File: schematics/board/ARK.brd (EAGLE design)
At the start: 82 x 92 mm, 82 parts, among them IC2 STM32F103C8T

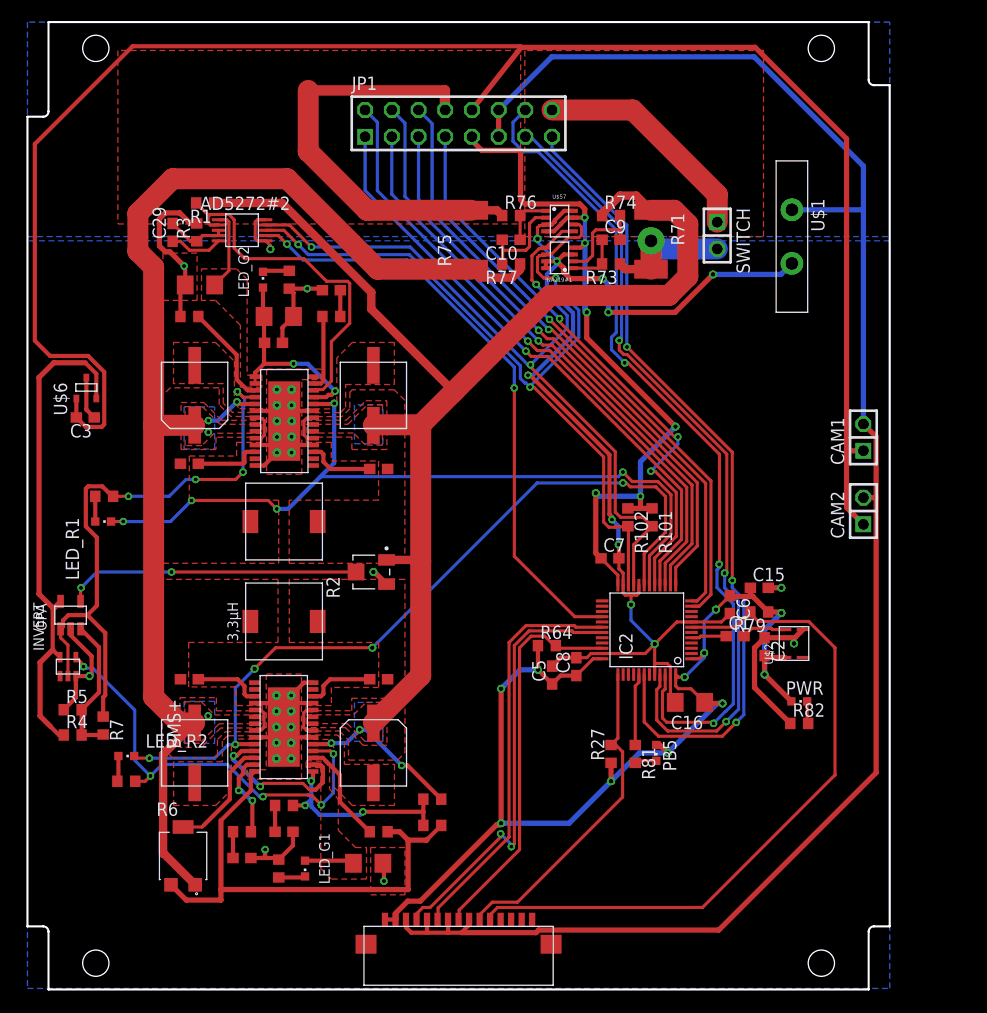
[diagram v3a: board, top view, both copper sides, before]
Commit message: Плата АРК готова к проверке
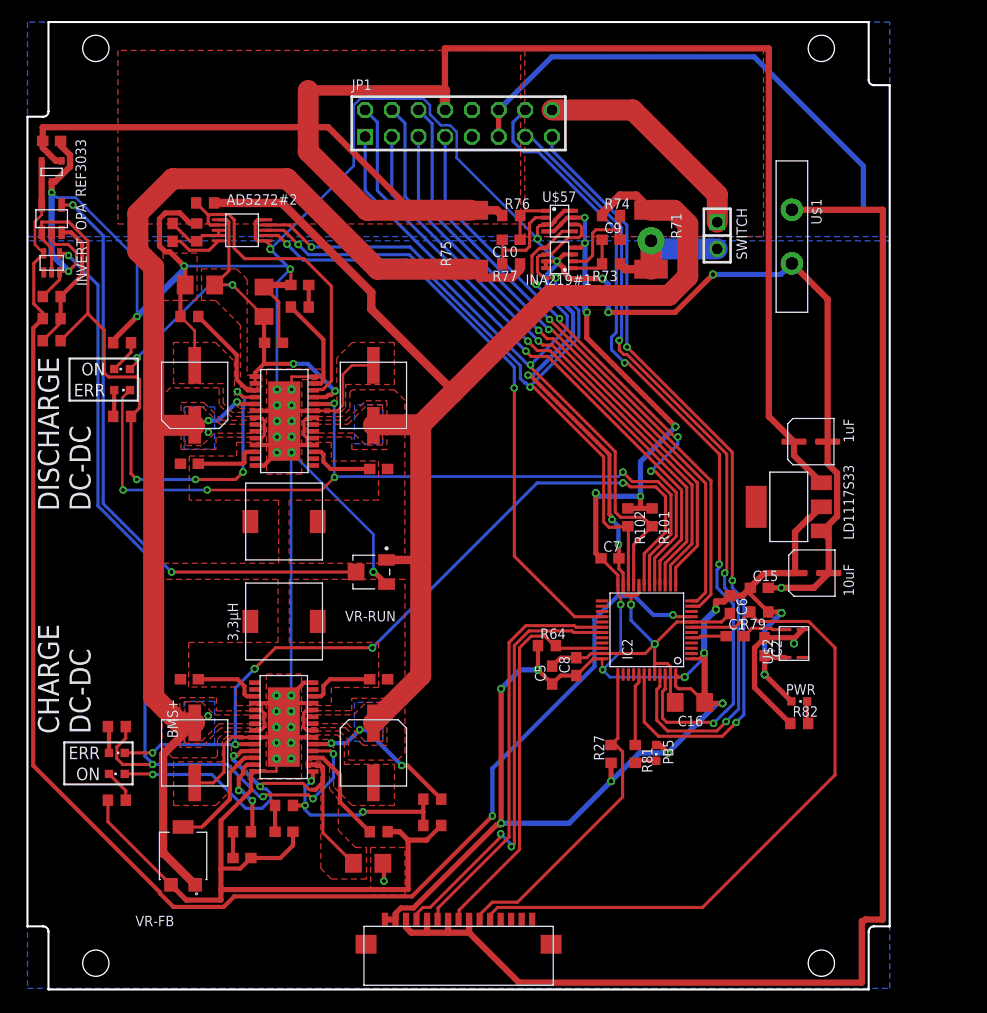
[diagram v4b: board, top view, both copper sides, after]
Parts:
- removed CAM1, CAM2: (no value), pinheadCS:1X02
- removed U$6: REF3033, CanCubeSat:SOT23-3
- added C11: 1uF, CanCubeSat:ECAP-SMD-D4
- added C4: 10uF, CanCubeSat:ECAP-SMD-D4
- added LD1117S33: LD1117S33, CanCubeSat:SOT223
- added REF3033: REF3033, CanCubeSat:SOT23-3
- moved R4 39.7 mm to (2.30, 63.8)
- moved R5 39.4 mm to (2.30, 65.9)
- moved INVERT 38.4 mm to (2.30, 69.1)
- moved OPA 37.7 mm to (2.30, 73.3)
- moved R7 36.9 mm to (2.30, 61.7), turned to 180 degrees
- moved C3 26.5 mm to (2.30, 80.7)
- moved LED_G1 20.0 mm to (8.50, 20.5), turned to 90 degrees
- moved R33 17.0 mm to (9.00, 61.5), turned to 0 degrees
- moved R100 16.7 mm to (8.50, 18.0), turned to 0 degrees
- moved LED_G2 15.9 mm to (9.00, 59.0), turned to 90 degrees
- moved LED_R1 12.6 mm to (9.00, 57.0)
- moved R32 7.79 mm to (9.00, 54.5)
- moved R57 5.28 mm to (8.50, 25.0)
- moved R30 3.13 mm to (25.9, 64.9)
- moved C52 3.04 mm to (25.9, 67.0)
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- renumbered R2 to VR-RUN, R6 to VR-FB
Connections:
- removed net 5V: C3.2, CAM1.1, CAM2.1, JP1.10, U$6.1
- new net 5V-OUT: JP1.10
- net 3V3: now also C4.P+, LD1117S33.P$3; no longer JP1.9
- net 3V3-STAB: now also REF3033.2; no longer U$6.2
- net BMS+: now also C11.P+, C3.2, LD1117S33.P$4, REF3033.1
- net GND: now also C11.P-, C4.P-, LD1117S33.P$2, REF3033.3; no longer U$6.3
- net GND-OUT: no longer CAM1.2, CAM2.2
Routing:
- net GND: track 254.5 -> 478.9 mm, vias 19 -> 20
- net 5V: track 167.7 -> 0.00 mm
- net BMS+: track 41.7 -> 162.6 mm
- net 3V3-STAB: track 47.0 -> 145.8 mm, vias 0 -> 2
- net Y: track 42.2 -> 83.6 mm
- net RUN: track 28.1 -> 57.4 mm
- net GND-OUT: track 165.9 -> 188.6 mm
- net N$234: track 20.0 -> 42.0 mm, vias 2 -> 3
- net 3V3: track 181.5 -> 199.8 mm, vias 17 -> 19
- net N$215: track 27.3 -> 43.7 mm, vias 2 -> 4
- net PGOOD2: track 75.9 -> 82.1 mm
- net A: track 57.8 -> 61.1 mm
- net N$3: track 33.3 -> 30.7 mm
- net N$81: track 7.21 -> 9.35 mm
- net N$92: track 2.54 -> 3.16 mm
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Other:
- board text added: "CHARGE DC-DC"
- board text added: "DISCHARGE DC-DC"
- board text added: "ERR"
- board text added: "ON"

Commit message: Украсил плату АРК
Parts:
- added U$3, U$4: PCB-"ARK", CanCubeSat:ITS-LOGO
- moved SWITCH 40.5 mm to (26.6, 82.7)
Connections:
- removed net 5V-OUT: JP1.10
- removed net BUSPLUS: JP1.16, SWITCH.1
- new net BMS+_OUT: JP1.8, SWITCH.1
- net BMS+: now also SWITCH.2; no longer JP1.8
- net BUS+: now also JP1.16; no longer SWITCH.2
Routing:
- net BUSPLUS: track 21.7 -> 0.00 mm
- net BUS+: track 12.5 -> 33.0 mm, vias 1 -> 2
- net BMS+_OUT: track 0.00 -> 17.5 mm
- net BMS+: track 162.6 -> 148.2 mm
- net INA_BUS+: track 131.1 -> 137.2 mm, vias 3 -> 5
- added copper zone on layer 1, net BUS+
- removed copper zone on layer 1, net BUSPLUS
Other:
- board text removed: "LTC3119"
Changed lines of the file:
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@@
 <layer number="25" name="tNames" color="7" fill="1" visible="yes" active="yes"/>
 <layer number="26" name="bNames" color="7" fill="1" visible="yes" active="yes"/>
-<layer number="27" name="tValues" color="7" fill="1" visible="yes" active="yes"/>
-<layer number="28" name="bValues" color="7" fill="1" visible="yes" active="yes"/>
+<layer number="27" name="tValues" color="7" fill="1" visible="no" active="yes"/>
+<layer number="28" name="bValues" color="7" fill="1" visible="no" active="yes"/>
 <layer number="29" name="tStop" color="7" fill="3" visible="no" active="yes"/>
 <layer number="30" name="bStop" color="7" fill="6" visible="no" active="yes"/>
@@
 <plain>
 <text x="13.3" y="27.63" size="1" layer="25" ratio="15" rot="R270">BMS+</text>
-<text x="39.5" y="47.6" size="1" layer="26" ratio="15" rot="MR180">LTC3119</text>
 <hole x="6.5" y="2.5" drill="2.5"/>
 <hole x="75.5" y="2.5" drill="2.5"/>
@@
 </element>
 <element name="VR-FB" library="CanCubeSat" package="TRIM_3314G-1-504E" value="3314G-1-504E" x="14.8" y="12.7" smashed="yes">
-<attribute name="NAME" x="10.26" y="6.01" size="1" layer="25" ratio="15"/>
-<attribute name="VALUE" x="10.26" y="7.62" size="1" layer="27" ratio="15"/>
-</element>
-<element name="SWITCH" library="pinheadCS" package="1X02" value="" x="65.6" y="71.7" smashed="yes" rot="R270">
-<attribute name="NAME" x="67.4288" y="74.3162" size="1" layer="25" ratio="15" rot="R270"/>
-<attribute name="VALUE" x="62.425" y="74.24" size="1.27" layer="27" rot="R270"/>
+<attribute name="NAME" x="18.39" y="10.76" size="1" layer="25" ratio="15" rot="R90"/>
+<attribute name="VALUE" x="11.38" y="10.76" size="1" layer="27" ratio="15" rot="R90"/>
+</element>
+<element name="SWITCH" library="pinheadCS" package="1X02" value="" x="26.6" y="82.7" smashed="yes" rot="R270">
+<attribute name="NAME" x="28.4288" y="85.3162" size="1" layer="25" ratio="15" rot="R270"/>
+<attribute name="VALUE" x="23.425" y="85.24" size="1.27" layer="27" rot="R270"/>
 </element>
 <element name="U$1" library="CanCubeSat" package="MF-R400" value="MF-R400" x="72.7" y="71.6" smashed="yes" rot="R180">
@@
 <element name="C11" library="CanCubeSat" package="ECAP-SMD-D4" value="1uF" x="74.5" y="52.1" smashed="yes" rot="R90">
 <attribute name="VALUE" x="78.6" y="52" size="1" layer="21" ratio="15" rot="R90"/>
+</element>
+<element name="U$3" library="CanCubeSat" package="ITS-LOGO" value="PCB-&quot;ARK&quot;" x="10" y="3" smashed="yes">
+<attribute name="VALUE" x="10" y="1.5" size="1" layer="21" font="vector" ratio="15"/>
+</element>
+<element name="U$4" library="CanCubeSat" package="ITS-LOGO" value="PCB-&quot;ARK&quot;" x="70.5" y="4.5" smashed="yes" rot="MR0">
+<attribute name="VALUE" x="70.5" y="3" size="1" layer="22" font="vector" ratio="15" rot="MR0"/>
 </element>
 </elements>
@@
 <wire x1="27.2" y1="51.78" x2="25.85" y2="51.78" width="0.4" layer="1"/>
 <wire x1="25.85" y1="51.78" x2="25.125" y2="51.055" width="0.4" layer="1"/>
-<wire x1="24.9" y1="67.15" x2="25.05" y2="67" width="0.4" layer="1"/>
 <wire x1="27.2" y1="55.03" x2="25.65" y2="55.03" width="0.4" layer="1"/>
 <wire x1="25.65" y1="55.03" x2="25.125" y2="55.555" width="0.4" layer="1"/>
@@
 <wire x1="32.7" y1="64.7" x2="40.55" y2="56.85" width="0.8" layer="1"/>
 <wire x1="32.7" y1="66.3" x2="32.7" y2="64.7" width="0.8" layer="1"/>
+<wire x1="27.2" y1="53.73" x2="31.5" y2="53.73" width="0.6" layer="1"/>
+<wire x1="31.5" y1="53.73" x2="31.5" y2="53" width="0.6" layer="1"/>
+<via x="31.5" y="53" extent="1-16" drill="0.35"/>
+<wire x1="31.5" y1="53" x2="31.5" y2="54" width="0.6" layer="16"/>
+<via x="31.5" y="54" extent="1-16" drill="0.35"/>
 </signal>
 <signal name="90">
@@
 <wire x1="28.1" y1="19.7" x2="28.1" y2="21.13573125" width="0.4" layer="1"/>
 <wire x1="28.1" y1="21.13573125" x2="27.85833125" y2="21.3774" width="0.4" layer="1"/>
-<wire x1="31" y1="12" x2="30.75" y2="12.25" width="0.4" layer="1"/>
 <polygon width="0.1524" layer="1" thermals="no">
 <vertex x="26.5" y="21.75"/>
@@
 <contactref element="R71" pad="2"/>
 <contactref element="R73" pad="1"/>
-<contactref element="SWITCH" pad="2"/>
 <wire x1="56.35" y1="69" x2="56.85" y2="68.5" width="0.8" layer="1"/>
 <wire x1="56.85" y1="68.5" x2="59.3" y2="68.5" width="0.8" layer="1"/>
 <wire x1="59.3" y1="68.5" x2="59.3" y2="71.2" width="2" layer="1"/>
 <via x="59.3" y="71.2" extent="1-16" drill="1.2" diameter="2.6"/>
-<wire x1="59.3" y1="71.2" x2="60.07" y2="70.43" width="2" layer="16"/>
-<wire x1="60.07" y1="70.43" x2="65.6" y2="70.43" width="2" layer="16"/>
+<wire x1="65.6" y1="75.6" x2="57.56" y2="83.64" width="2" layer="1"/>
+<polygon width="0.1524" layer="1" thermals="no">
+<vertex x="47.3" y="89.3"/>
+<vertex x="47.3" y="71.6"/>
+<vertex x="70" y="71.6"/>
+<vertex x="70" y="89.3"/>
+</polygon>
+<contactref element="JP1" pad="16"/>
+<wire x1="57.56" y1="83.64" x2="49.89" y2="83.64" width="2" layer="1"/>
+<wire x1="59.3" y1="71.2" x2="63.7" y2="75.6" width="2" layer="16"/>
+<wire x1="63.7" y1="75.6" x2="65.6" y2="75.6" width="2" layer="16"/>
+<via x="65.6" y="75.6" extent="1-16" drill="1.2" diameter="2.6"/>
 </signal>
 <signal name="N$159">
@@
 <wire x1="58" y1="21.75" x2="59.8" y2="21.75" width="0.3" layer="1"/>
 </signal>
-<signal name="BUSPLUS">
-<contactref element="SWITCH" pad="1"/>
-<wire x1="65.6" y1="72.97" x2="65.6" y2="75.6" width="2" layer="1"/>
-<wire x1="65.6" y1="75.6" x2="57.56" y2="83.64" width="2" layer="1"/>
-<polygon width="0.1524" layer="1">
-<vertex x="47.3" y="89.3"/>
-<vertex x="47.3" y="71.6"/>
-<vertex x="70" y="71.6"/>
-<vertex x="70" y="89.3"/>
-</polygon>
-<contactref element="JP1" pad="16"/>
-<wire x1="57.56" y1="83.64" x2="49.89" y2="83.64" width="2" layer="1"/>
-</signal>
 <signal name="SWC">
 <contactref element="R27" pad="2"/>
@@
 <contactref element="R75" pad="2"/>
 <contactref element="R76" pad="1"/>
-<contactref element="JP1" pad="8"/>
-<wire x1="42.2" y1="74.1" x2="44.65" y2="74.1" width="0.8" layer="1"/>
+<wire x1="44.65" y1="74.1" x2="42.2" y2="74.1" width="0.8" layer="1"/>
 <wire x1="44.65" y1="74.1" x2="45.15" y2="73.6" width="0.8" layer="1"/>
 <polygon width="0.1524" layer="1">
@@
 <vertex x="46.9" y="89.3"/>
 </polygon>
-<wire x1="26.7" y1="85.5" x2="39.7" y2="85.5" width="1" layer="1"/>
-<wire x1="39.7" y1="85.5" x2="39.7" y2="83.640975" width="1" layer="1"/>
-<wire x1="39.7" y1="83.640975" x2="39.73" y2="83.64" width="1" layer="1"/>
-<wire x1="42.2" y1="74.1" x2="36.5" y2="74.1" width="2" layer="1"/>
-<wire x1="36.5" y1="74.1" x2="32.3" y2="74.1" width="2" layer="1"/>
-<wire x1="26.7" y1="85.5" x2="26.7" y2="79.7" width="2" layer="1"/>
-<wire x1="32.3" y1="74.1" x2="26.7" y2="79.7" width="2" layer="1"/>
 <contactref element="REF3033" pad="1"/>
 <contactref element="C3" pad="2"/>
 <contactref element="LD1117S33" pad="P$4"/>
 <contactref element="C11" pad="P+"/>
-<wire x1="26.7" y1="79.7" x2="26.7" y2="79.5" width="0.6" layer="1"/>
 <wire x1="1.45" y1="80.05210625" x2="1.45" y2="80.7" width="0.6" layer="1"/>
 <wire x1="3.25" y1="78.8" x2="2.70210625" y2="78.8" width="0.6" layer="1"/>
 <wire x1="2.70210625" y1="78.8" x2="1.45" y2="80.05210625" width="0.6" layer="1"/>
 <wire x1="1.45" y1="80.7" x2="1.45" y2="82" width="0.6" layer="1"/>
-<wire x1="28.6" y1="82" x2="36.5" y2="74.1" width="0.6" layer="1"/>
-<wire x1="1.45" y1="82" x2="28.6" y2="82" width="0.6" layer="1"/>
 <wire x1="75.5" y1="48.19" x2="72.9" y2="50.79" width="0.6" layer="1"/>
 <wire x1="72.9" y1="50.79" x2="72.9" y2="52.1" width="0.6" layer="1"/>
 <wire x1="72.9" y1="52.1" x2="70.5" y2="54.5" width="0.6" layer="1"/>
 <wire x1="70.5" y1="54.5" x2="70.5" y2="89.5" width="0.6" layer="1"/>
-<wire x1="39.7" y1="89.5" x2="39.7" y2="85.5" width="0.6" layer="1"/>
-<wire x1="70.5" y1="89.5" x2="39.7" y2="89.5" width="0.6" layer="1"/>
+<contactref element="SWITCH" pad="2"/>
+<wire x1="26.6" y1="81.43" x2="33.93" y2="74.1" width="2" layer="1"/>
+<wire x1="33.93" y1="74.1" x2="42.2" y2="74.1" width="2" layer="1"/>
+<wire x1="26.6" y1="81.43" x2="25" y2="81.43" width="0.6" layer="1"/>
+<wire x1="70.5" y1="89.5" x2="25" y2="89.5" width="0.6" layer="1"/>
+<wire x1="25" y1="89.5" x2="25" y2="82" width="0.6" layer="1"/>
+<wire x1="25" y1="82" x2="25" y2="81.43" width="0.6" layer="1"/>
+<wire x1="1.45" y1="82" x2="25" y2="82" width="0.6" layer="1"/>
 </signal>
 <signal name="N$150">
@@
 <wire x1="3.15" y1="63.4" x2="3.15" y2="63.8" width="0.3" layer="1"/>
 </signal>
-<signal name="5V-OUT">
-<contactref element="JP1" pad="10"/>
+<signal name="BMS+_OUT">
+<contactref element="SWITCH" pad="1"/>
+<contactref element="JP1" pad="8"/>
+<wire x1="26.6" y1="83.97" x2="26.6" y2="86" width="2" layer="1"/>
+<wire x1="39.73" y1="86" x2="39.73" y2="83.64" width="2" layer="1"/>
+<wire x1="26.6" y1="86" x2="39.73" y2="86" width="2" layer="1"/>
 </signal>
 </signals>

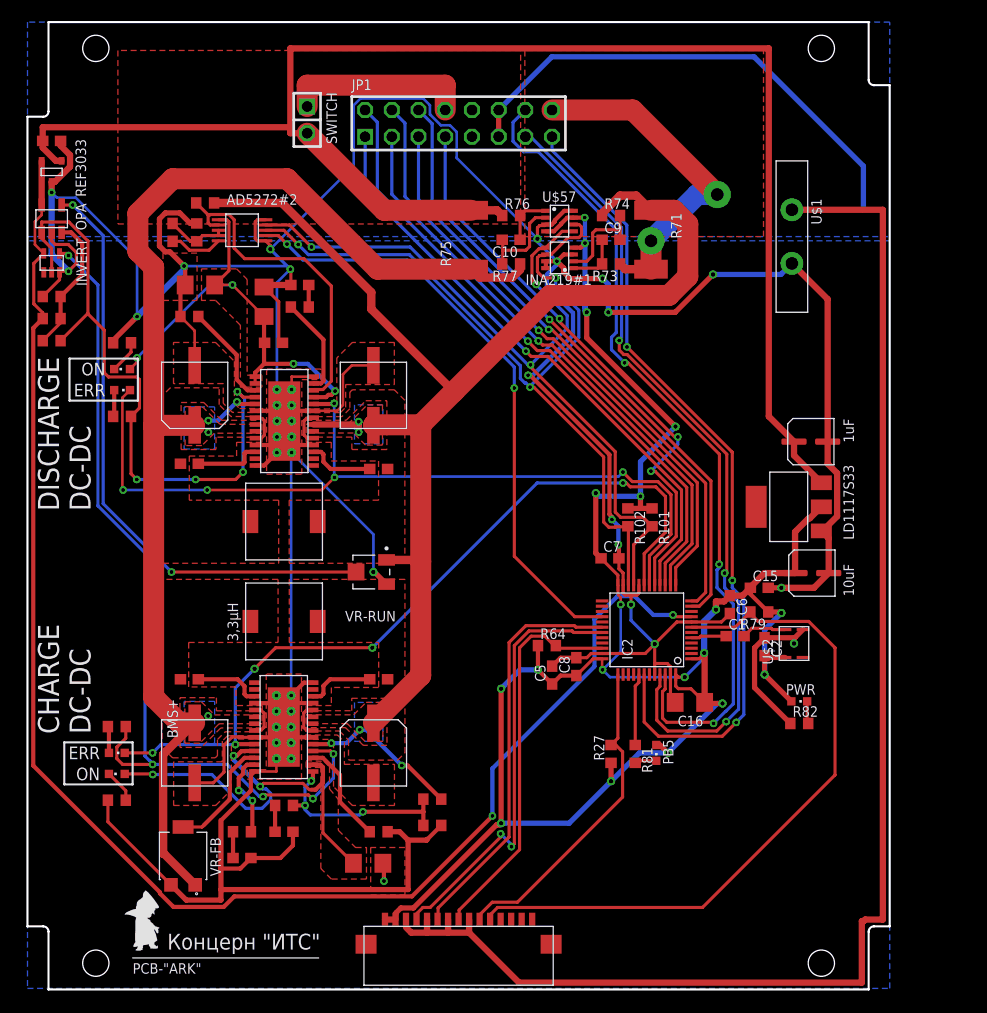
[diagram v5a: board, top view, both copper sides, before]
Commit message: Завершена разработка плат БСК5 и АРК, половина платы БКУ разведена, добавлены гербер файлы плат АРК, БСК5 и WSPR
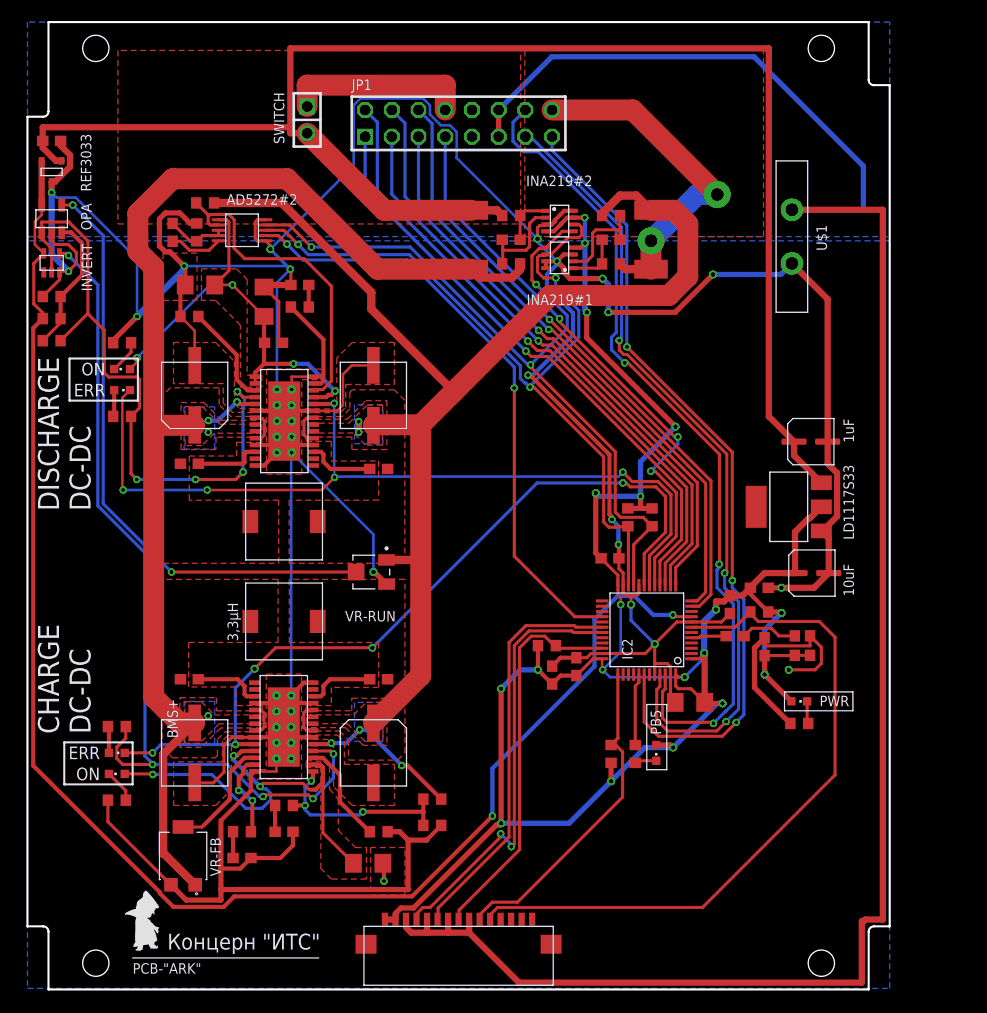
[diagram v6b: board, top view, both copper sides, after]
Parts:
- removed U$2: Q24, CanCubeSat:Q24
- added TCXO: OC2E08000XCCDRX, CanCubeSat:OC2E08000XCCDRX
- renumbered U$57 to INA219#2
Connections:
- net 3V3: now also TCXO.P$1, TCXO.P$4; no longer U$2.P$4
- net GND: now also TCXO.P$2; no longer U$2.P$2
- net N$4: now also TCXO.P$3; no longer U$2.P$3
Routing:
- net GND: track 478.7 -> 486.6 mm
- net INA_BUS+: track 137.2 -> 132.9 mm
- net 3V3: track 199.8 -> 202.4 mm
- net N$4: track 4.26 -> 5.44 mm
- net NRST: track 66.6 -> 67.2 mm
